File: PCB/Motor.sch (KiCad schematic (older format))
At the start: 30 parts, among them J201 SW2, M201 Stepper_Motor_bipolar, U201 L6470_HTSSOP28

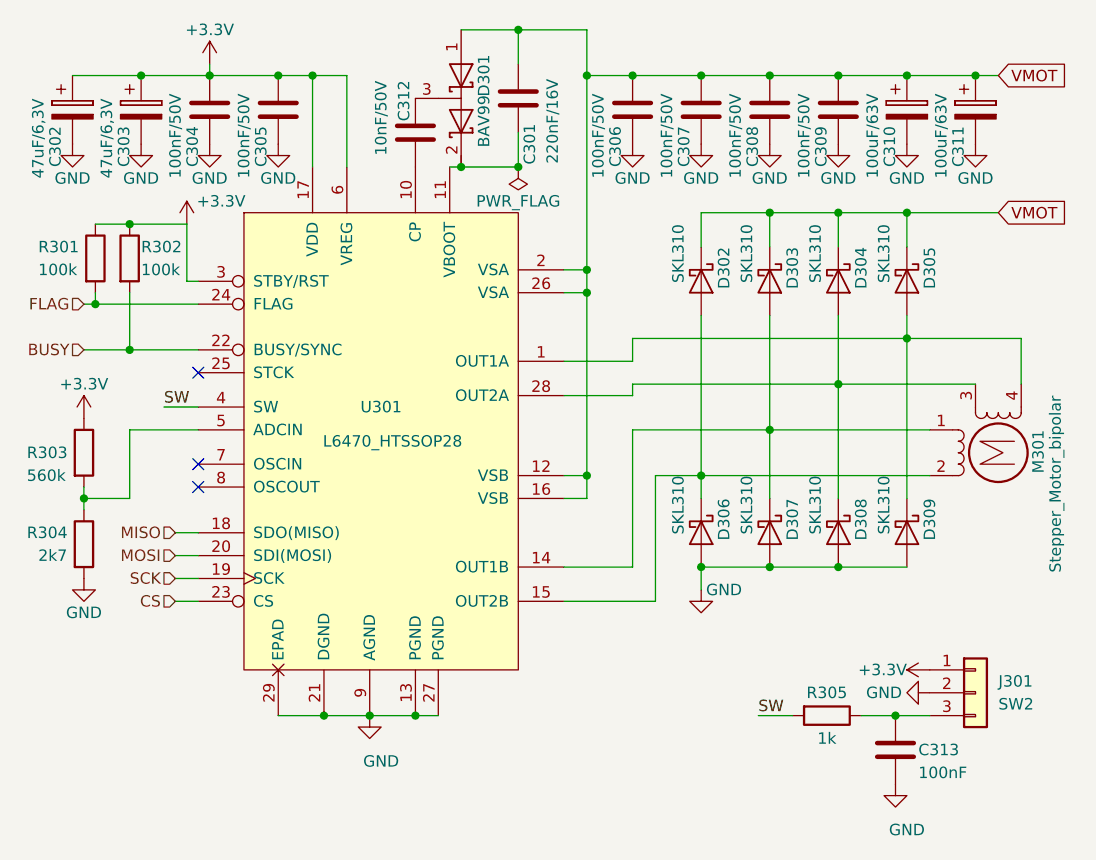
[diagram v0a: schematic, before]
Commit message: PCB: route current meter, reverse polarity protection, stepdown converter
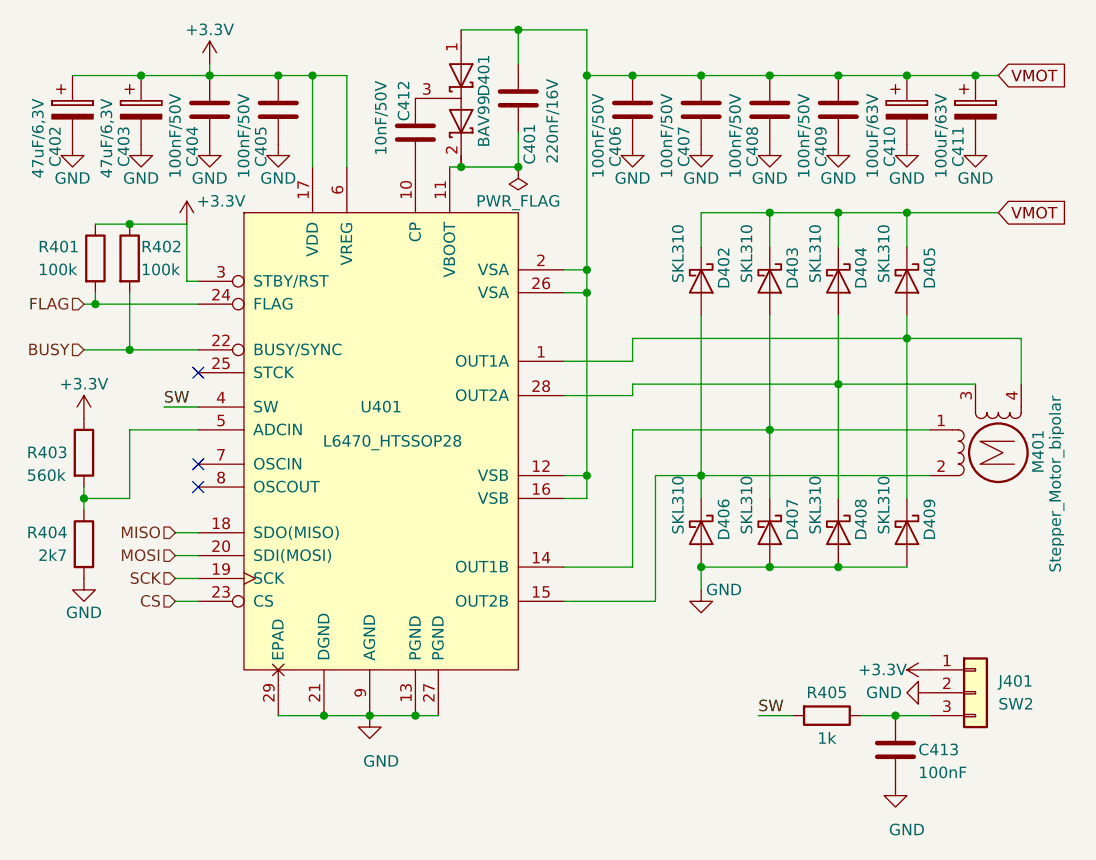
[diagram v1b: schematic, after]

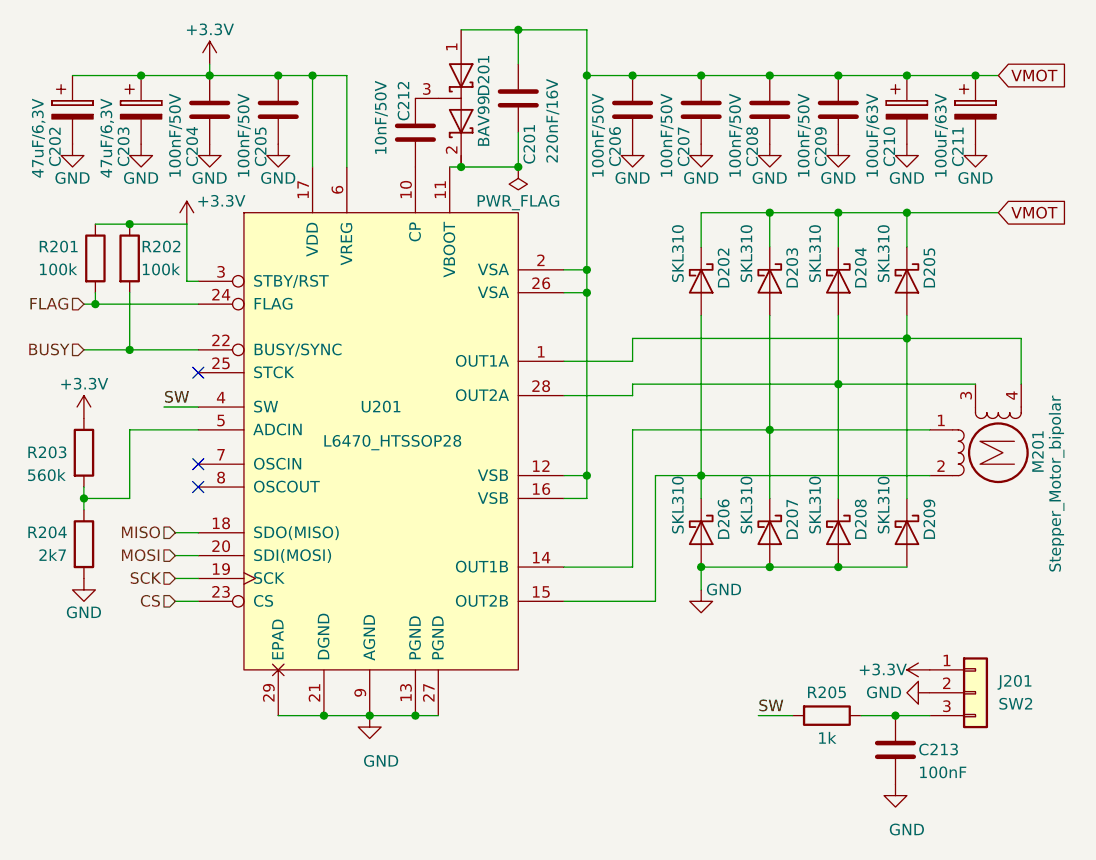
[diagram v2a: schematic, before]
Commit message: PCB: create new layout for power supply, route LED signalization and reset
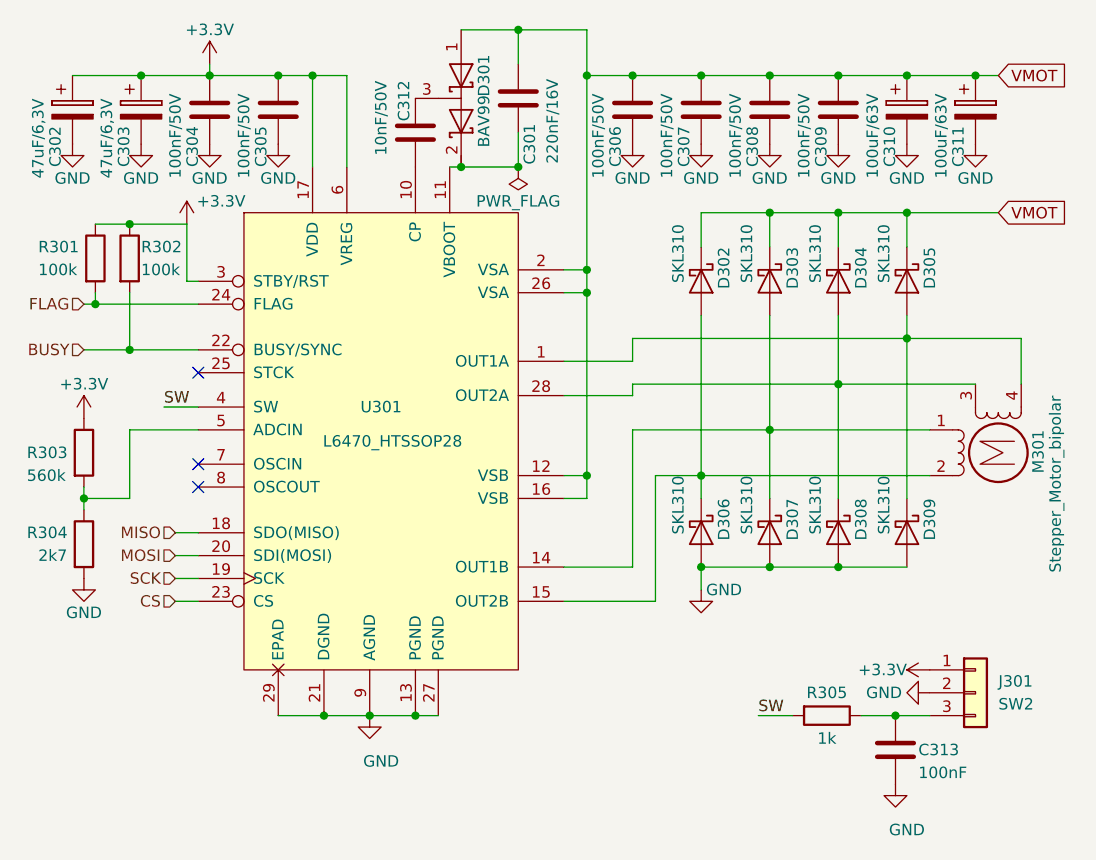
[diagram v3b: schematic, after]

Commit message: PCB: change programing and debugging IDC connectors to vertical version
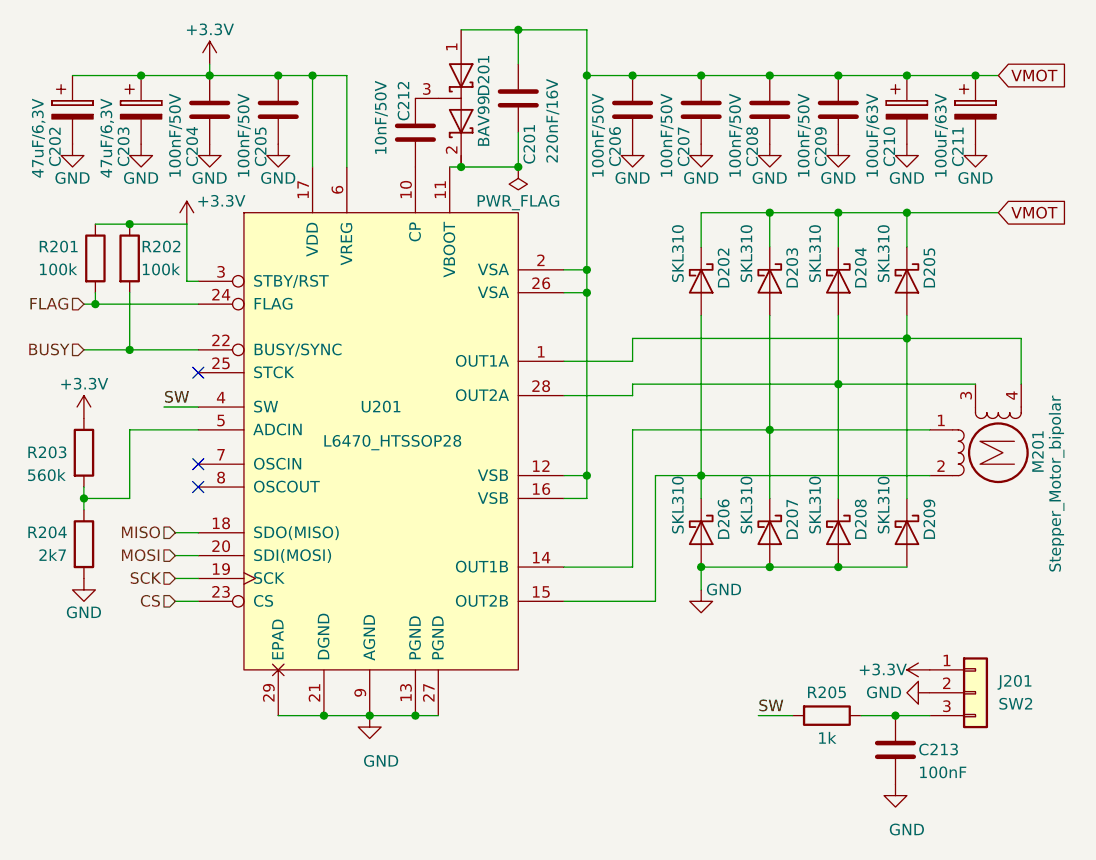
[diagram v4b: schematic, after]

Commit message: PCB: change package size of USB ferrite from 1206 to 0803
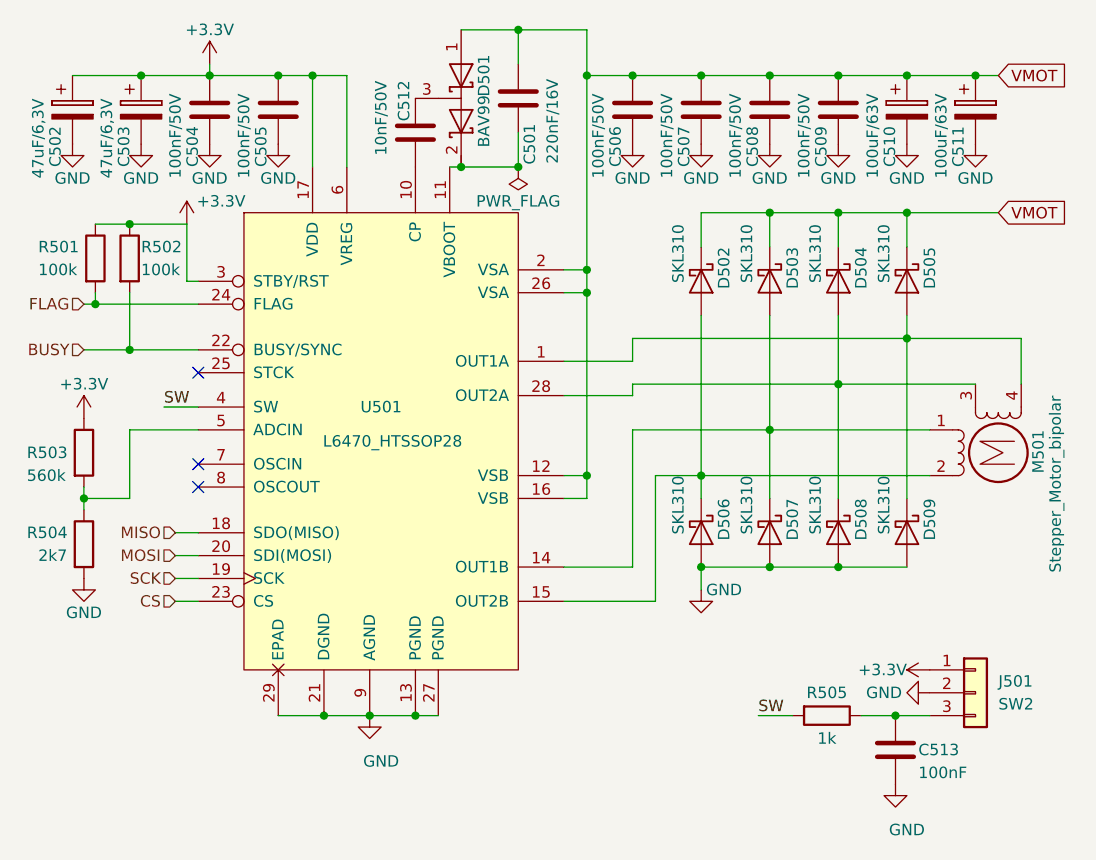
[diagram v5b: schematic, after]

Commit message: Schema & PCB: add routing of MCu connection, debug and extension port
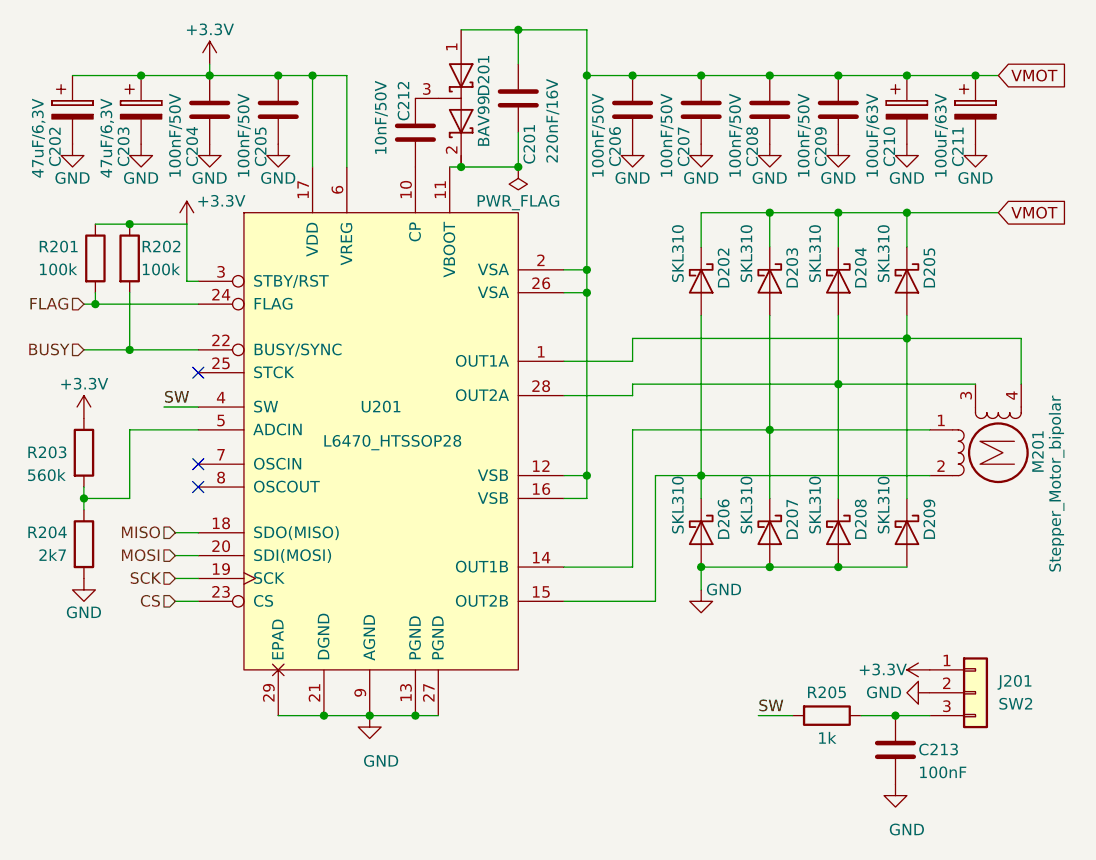
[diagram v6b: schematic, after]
